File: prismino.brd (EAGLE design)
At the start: 50 x 50 mm, 31 parts, among them IC1 NCP1117DT05BDTRKG, J1 ISP-6PIN, Q1 16MHz, U1 ATMEGA32U4

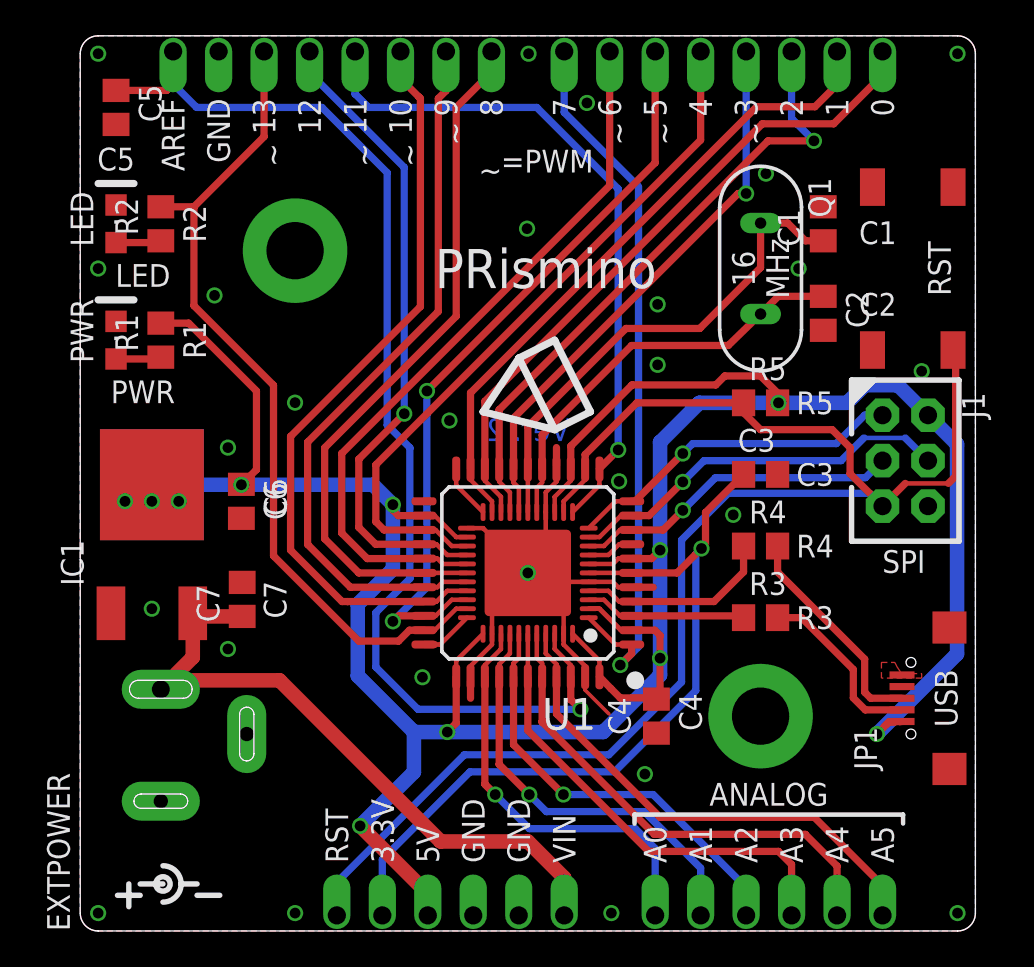
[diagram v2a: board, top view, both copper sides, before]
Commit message: Added a solder jumper and updated everything
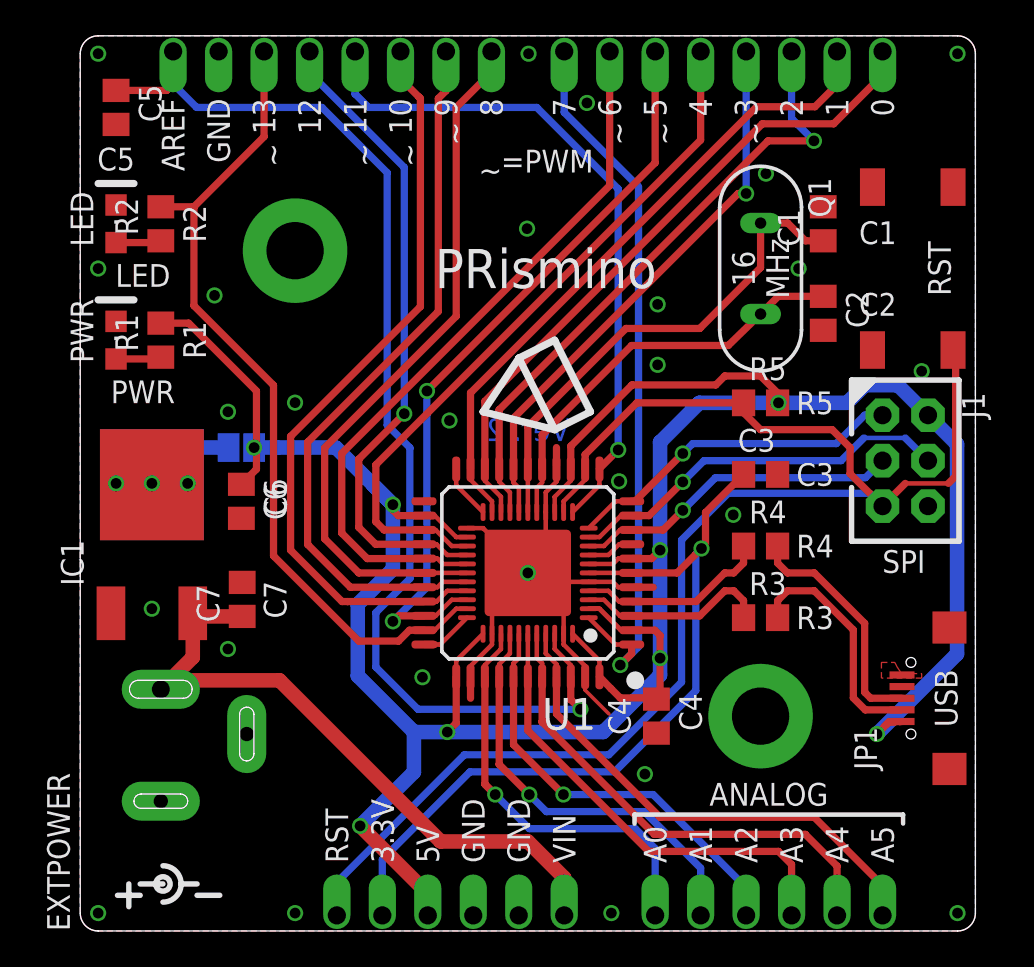
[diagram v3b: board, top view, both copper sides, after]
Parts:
- added SJ1: (no value), robopoly:SJ
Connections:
- new net N$1: IC1.HEATSINK, IC1.PAD, SJ1.1
- net VCC: now also SJ1.2; no longer IC1.2, IC1.PAD
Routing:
- net VCC: track 181.0 -> 172.0 mm, vias 11 -> 8
- net N$1: track 0.00 -> 5.15 mm
- net N$6: track 10.0 -> 13.1 mm
- net DM: track 9.09 -> 10.8 mm
- net N$7: track 12.4 -> 13.3 mm
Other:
- board text added: "2014-07-24"
- board text removed: "2014-03-04"
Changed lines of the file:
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@@
 <layer number="49" name="Reference" color="7" fill="1" visible="no" active="yes"/>
 <layer number="50" name="dxf" color="7" fill="1" visible="no" active="no"/>
-<layer number="51" name="tDocu" color="7" fill="1" visible="no" active="yes"/>
-<layer number="52" name="bDocu" color="7" fill="1" visible="no" active="yes"/>
+<layer number="51" name="tDocu" color="7" fill="1" visible="yes" active="yes"/>
+<layer number="52" name="bDocu" color="7" fill="1" visible="yes" active="yes"/>
 <layer number="53" name="tGND_GNDA" color="7" fill="9" visible="no" active="no"/>
 <layer number="54" name="bGND_GNDA" color="1" fill="9" visible="no" active="no"/>
@@
 <text x="0" y="-3" size="1.778" layer="48" font="vector" ratio="12">PRismino</text>
 <text x="50" y="-3" size="1.778" layer="48" font="vector" ratio="12" align="bottom-right">Version: 2</text>
-<text x="50" y="-6" size="1.27" layer="48" font="vector" ratio="12" align="bottom-right">2014-03-04</text>
+<text x="50" y="-6" size="1.27" layer="48" font="vector" ratio="12" align="bottom-right">2014-07-24</text>
 <text x="0" y="-6" size="1.27" layer="48" font="vector" ratio="12">http://robopoly.epfl.ch</text>
 <text x="0" y="-9" size="1.27" layer="48" font="vector" ratio="12">Licence: CC-BY-SA</text>
+<text x="9" y="25.5" size="1.27" layer="22" font="vector" ratio="12" rot="MR0" align="top-center">5V</text>
 </plain>
 <attributes>
@@
 <element name="BY1" library="robopoly" package="BY" value="BYBOTTOM" x="46" y="13"/>
 <element name="SA1" library="robopoly" package="SA" value="SABOTTOM" x="46" y="8.5"/>
+<element name="SJ1" library="robopoly" package="SJ" value="" x="9" y="27" rot="MR180"/>
 </elements>
 <signals>
@@
 <contactref element="R1" pad="2"/>
 <contactref element="PIN1" pad="3"/>
-<contactref element="IC1" pad="2"/>
 <contactref element="C6" pad="1"/>
 <contactref element="R5" pad="2"/>
@@
 <wire x1="9.8425" y1="30.1625" x2="6.055" y2="33.95" width="0.4064" layer="1"/>
 <wire x1="6.055" y1="33.95" x2="4.5" y2="33.95" width="0.4064" layer="1"/>
-<contactref element="IC1" pad="PAD"/>
-<via x="2.5" y="24" extent="1-16" drill="0.6" shape="octagon"/>
-<via x="4" y="24" extent="1-16" drill="0.6" shape="octagon"/>
-<via x="5.5" y="24" extent="1-16" drill="0.6" shape="octagon"/>
-<wire x1="4" y1="24" x2="2.5" y2="24" width="0.8128" layer="1"/>
-<wire x1="4" y1="24.925" x2="4" y2="24" width="0.8128" layer="1"/>
-<wire x1="4" y1="24" x2="5.5" y2="24" width="0.8128" layer="1"/>
-<wire x1="4" y1="24.925" x2="4.575" y2="24.925" width="0.8128" layer="16"/>
-<wire x1="4.575" y1="24.925" x2="5.5" y2="24" width="0.8128" layer="16"/>
 <via x="20.5" y="11.1125" extent="1-16" drill="0.6" shape="octagon"/>
 <wire x1="21" y1="14.2" x2="21" y2="11.6125" width="0.4064" layer="1"/>
@@
 <via x="39" y="29.5" extent="1-16" drill="0.6" shape="octagon"/>
 <wire x1="48.977" y1="15.477" x2="48.977" y2="27.185" width="0.8128" layer="16"/>
-<wire x1="4" y1="24.925" x2="6.45" y2="24.925" width="0.8128" layer="16"/>
-<wire x1="6.45" y1="24.925" x2="9" y2="24.925" width="0.8128" layer="16"/>
-<wire x1="9" y1="24.925" x2="16.35" y2="24.925" width="0.8128" layer="16"/>
 <wire x1="16.35" y1="24.925" x2="17.4625" y2="23.8125" width="0.8128" layer="16"/>
-<wire x1="5.5" y1="24" x2="6.45" y2="24.925" width="0.4064" layer="16"/>
-<via x="9" y="24.925" extent="1-16" drill="0.6" shape="octagon"/>
-<wire x1="9.8425" y1="25.7675" x2="9.8425" y2="30.1625" width="0.4064" layer="1"/>
-<wire x1="9.8425" y1="25.7675" x2="9" y2="24.925" width="0.4064" layer="1"/>
 <wire x1="17.4625" y1="23.8125" x2="17.4625" y2="20.2125" width="0.8128" layer="16"/>
 <wire x1="17.4625" y1="20.2125" x2="15.5" y2="18.25" width="0.8128" layer="16"/>
@@
 <wire x1="18.6375" y1="11.1125" x2="18.6375" y2="8.8735" width="0.8128" layer="16"/>
 <wire x1="39" y1="29.5" x2="38.95" y2="29.5" width="0.4064" layer="1"/>
-<wire x1="9" y1="24.95" x2="9" y2="24.925" width="0.4064" layer="1"/>
+<contactref element="SJ1" pad="2"/>
+<wire x1="9.75" y1="27" x2="11" y2="27" width="0.8128" layer="16"/>
+<wire x1="11" y1="27" x2="14.275" y2="27" width="0.8128" layer="16"/>
+<wire x1="14.275" y1="27" x2="17.4625" y2="23.8125" width="0.8128" layer="16"/>
+<wire x1="9.8425" y1="25.7925" x2="9" y2="24.95" width="0.4064" layer="1"/>
+<wire x1="9.8425" y1="26.8687" x2="9.8425" y2="30.1625" width="0.4064" layer="1"/>
+<wire x1="9.8425" y1="25.7925" x2="9.8425" y2="26.8687" width="0.4064" layer="1"/>
+<wire x1="9.8425" y1="26.8687" x2="9.7112" y2="27" width="0.4064" layer="1" curve="90"/>
+<via x="9.7112" y="27" extent="1-16" drill="0.6" shape="octagon"/>
+<wire x1="9.7112" y1="27" x2="11" y2="27" width="0.4064" layer="16"/>
 </signal>
 <signal name="A5">
@@
 <via x="4" y="18" extent="1-16" drill="0.6" shape="octagon"/>
 <via x="28.302" y="46.25" extent="1-16" drill="0.6" shape="octagon"/>
-<via x="8.25" y="27" extent="1-16" drill="0.6" shape="octagon"/>
+<via x="8.25" y="29" extent="1-16" drill="0.6" shape="octagon"/>
 <via x="8.25" y="15.75" extent="1-16" drill="0.6" shape="octagon"/>
 </signal>
@@
 <contactref element="R3" pad="1"/>
 <contactref element="U1" pad="3"/>
-<wire x1="37.015" y1="17.6" x2="37.05" y2="17.5" width="0.4064" layer="1"/>
 <contactref element="U1" pad="47"/>
-<wire x1="37.015" y1="17.6" x2="30.8" y2="17.6" width="0.4064" layer="1"/>
 <wire x1="28.4" y1="18.5" x2="29.25" y2="18.5" width="0.254" layer="1"/>
 <wire x1="29.25" y1="18.5" x2="30.15" y2="17.6" width="0.254" layer="1"/>
 <wire x1="30.15" y1="17.6" x2="30.8" y2="17.6" width="0.254" layer="1"/>
+<wire x1="30.8" y1="17.6" x2="34.6" y2="17.6" width="0.4064" layer="1"/>
+<wire x1="34.6" y1="17.6" x2="36" y2="19" width="0.4064" layer="1"/>
+<wire x1="36" y1="19" x2="36.5" y2="19" width="0.4064" layer="1"/>
+<wire x1="36.5" y1="19" x2="37.05" y2="18.45" width="0.4064" layer="1"/>
+<wire x1="37.05" y1="18.45" x2="37.05" y2="17.5" width="0.4064" layer="1"/>
 </signal>
 <signal name="DP">
@@
 <wire x1="29.5" y1="19" x2="30.1" y2="18.4" width="0.254" layer="1"/>
 <wire x1="30.1" y1="18.4" x2="30.8" y2="18.4" width="0.254" layer="1"/>
-<wire x1="30.8" y1="18.4" x2="35.4" y2="18.4" width="0.4064" layer="1"/>
-<wire x1="35.4" y1="18.4" x2="37.05" y2="20.05" width="0.4064" layer="1"/>
-<wire x1="37.05" y1="20.05" x2="37.05" y2="21.5" width="0.4064" layer="1"/>
+<wire x1="30.8" y1="18.4" x2="34.4" y2="18.4" width="0.4064" layer="1"/>
+<wire x1="34.4" y1="18.4" x2="36" y2="20" width="0.4064" layer="1"/>
+<wire x1="36" y1="20" x2="36.5" y2="20" width="0.4064" layer="1"/>
+<wire x1="36.5" y1="20" x2="37.05" y2="20.55" width="0.4064" layer="1"/>
+<wire x1="37.05" y1="20.55" x2="37.05" y2="21.5" width="0.4064" layer="1"/>
 </signal>
 <signal name="N$6">
 <contactref element="JP1" pad="D-"/>
 <contactref element="R3" pad="2"/>
-<wire x1="43.18" y1="14.605" x2="43.18" y2="13.0175" width="0.4064" layer="1"/>
+<wire x1="43.18" y1="16.82" x2="43.18" y2="13.0175" width="0.4064" layer="1"/>
 <wire x1="43.18" y1="13.0175" x2="43.8475" y2="12.35" width="0.4064" layer="1"/>
 <wire x1="43.8475" y1="12.35" x2="45.9" y2="12.35" width="0.4064" layer="1"/>
-<wire x1="43.18" y1="14.605" x2="40.285" y2="17.5" width="0.4064" layer="1"/>
-<wire x1="40.285" y1="17.5" x2="38.95" y2="17.5" width="0.4064" layer="1"/>
+<wire x1="43.18" y1="16.82" x2="41" y2="19" width="0.4064" layer="1"/>
+<wire x1="41" y1="19" x2="39.5" y2="19" width="0.4064" layer="1"/>
+<wire x1="39.5" y1="19" x2="38.95" y2="18.45" width="0.4064" layer="1"/>
+<wire x1="38.95" y1="18.45" x2="38.95" y2="17.5" width="0.4064" layer="1"/>
 </signal>
 <signal name="N$7">
@@
 <wire x1="44.15" y1="13" x2="45.9" y2="13" width="0.4064" layer="1"/>
 <wire x1="44.15" y1="13" x2="43.815" y2="13.335" width="0.4064" layer="1"/>
-<wire x1="43.815" y1="13.335" x2="43.815" y2="15.185" width="0.4064" layer="1"/>
-<wire x1="43.815" y1="15.185" x2="38.95" y2="20.05" width="0.4064" layer="1"/>
-<wire x1="38.95" y1="20.05" x2="38.95" y2="21.5" width="0.4064" layer="1"/>
+<wire x1="43.815" y1="13.335" x2="43.815" y2="17.185" width="0.4064" layer="1"/>
+<wire x1="43.815" y1="17.185" x2="41" y2="20" width="0.4064" layer="1"/>
+<wire x1="41" y1="20" x2="39.5" y2="20" width="0.4064" layer="1"/>
+<wire x1="39.5" y1="20" x2="38.95" y2="20.55" width="0.4064" layer="1"/>
+<wire x1="38.95" y1="20.55" x2="38.95" y2="21.5" width="0.4064" layer="1"/>
 </signal>
 <signal name="N$3">
@@
 <wire x1="16.872" y1="3.9895" x2="16.872" y2="0.87" width="0.4064" layer="16"/>
 </signal>
+<signal name="N$1">
+<contactref element="IC1" pad="HEATSINK"/>
+<contactref element="IC1" pad="PAD"/>
+<contactref element="SJ1" pad="1"/>
+<wire x1="8.2888" y1="27" x2="6.075" y2="27" width="0.8128" layer="16"/>
+<wire x1="6.075" y1="27" x2="4" y2="24.925" width="0.8128" layer="16"/>
+<wire x1="4" y1="24.925" x2="4" y2="24.925" width="0" layer="19" extent="1-16"/>
+</signal>
+<signal name="N$2">
+<via x="2" y="25" extent="1-16" drill="0.6" shape="octagon"/>
+</signal>
+<signal name="N$4">
+<via x="4" y="25" extent="1-16" drill="0.6" shape="octagon"/>
+</signal>
+<signal name="N$5">
+<via x="6" y="25" extent="1-16" drill="0.6" shape="octagon"/>
+</signal>
 </signals>
